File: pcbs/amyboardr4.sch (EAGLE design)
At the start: 126 parts, among them J1 52601-G10-8LF, Q2 S8050, Q5 S8050, U1 PCM9211PT, U13 HX3608, U15 H11L1SR2M, U16 SPX3819, U2 ESP32­S2­SOLO, Y1 22.5792MHZ

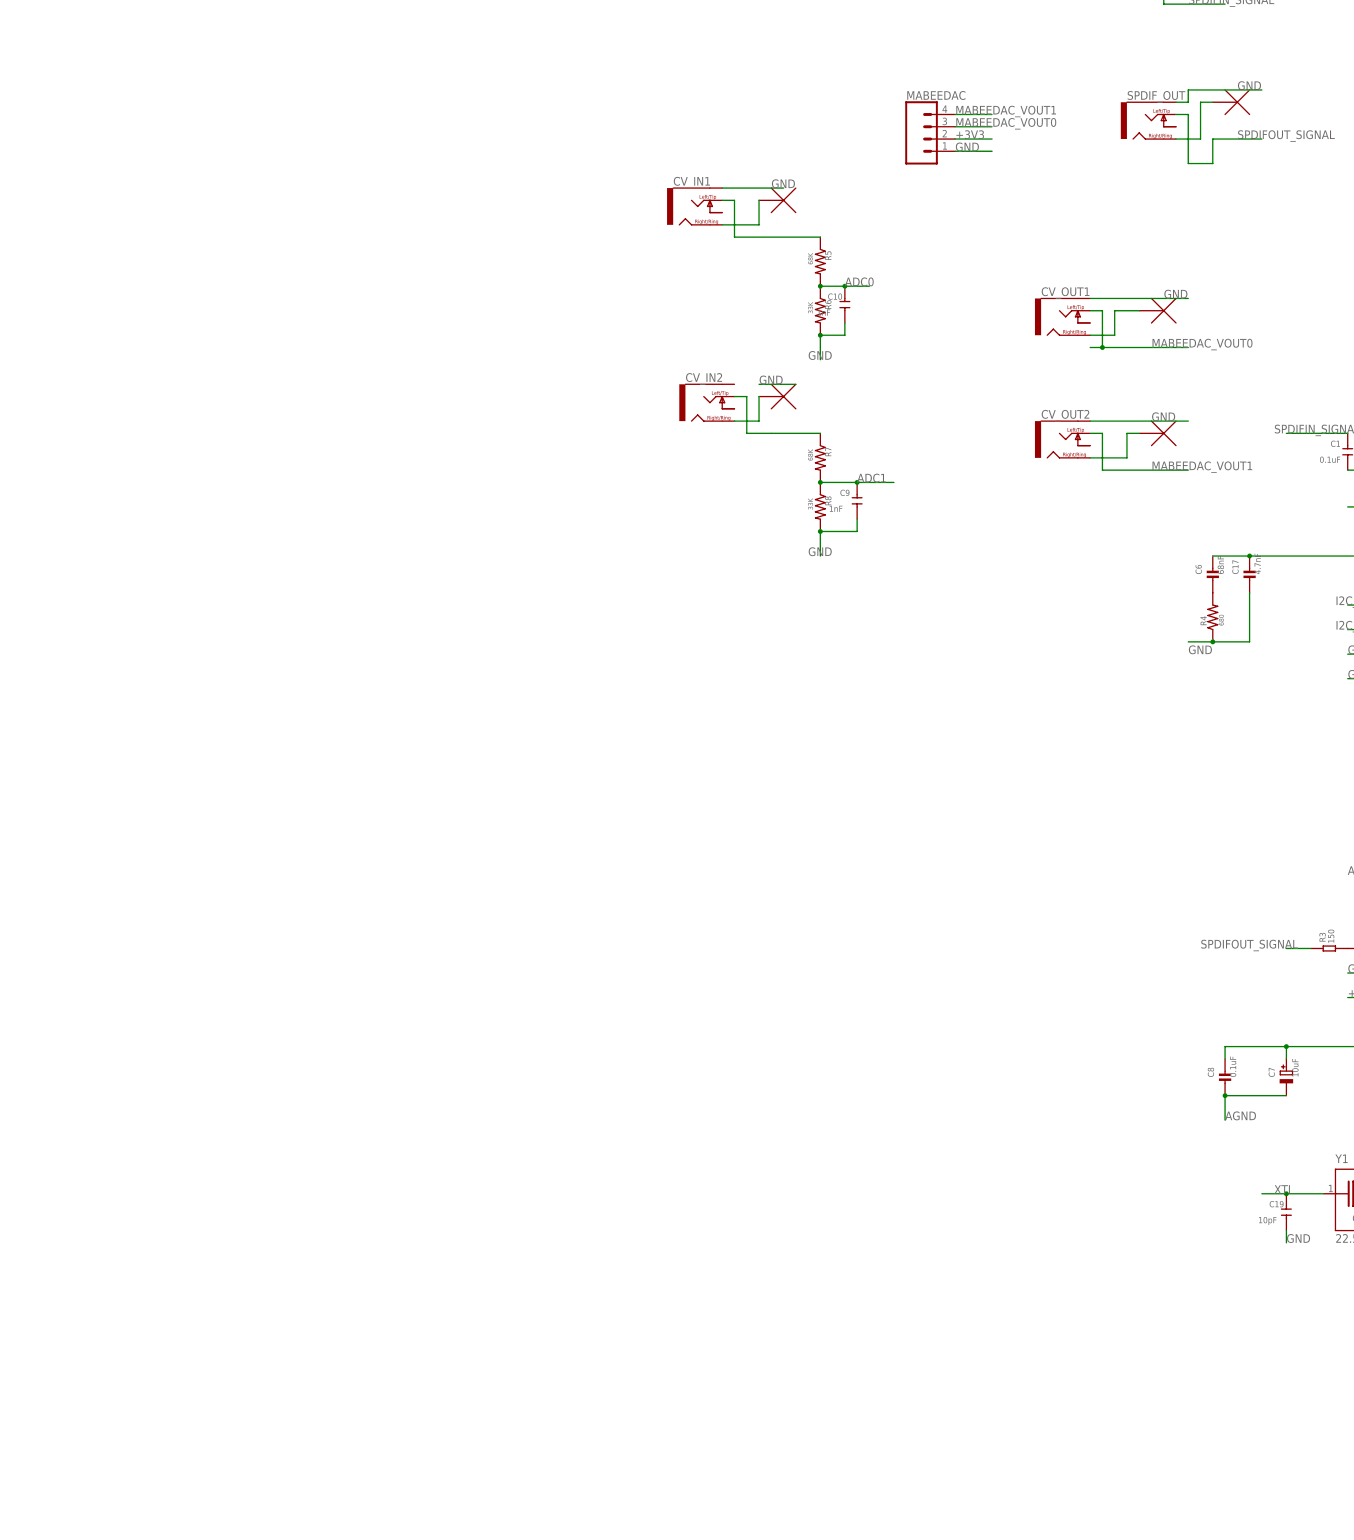
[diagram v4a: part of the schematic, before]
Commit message: adding parts for amyboard
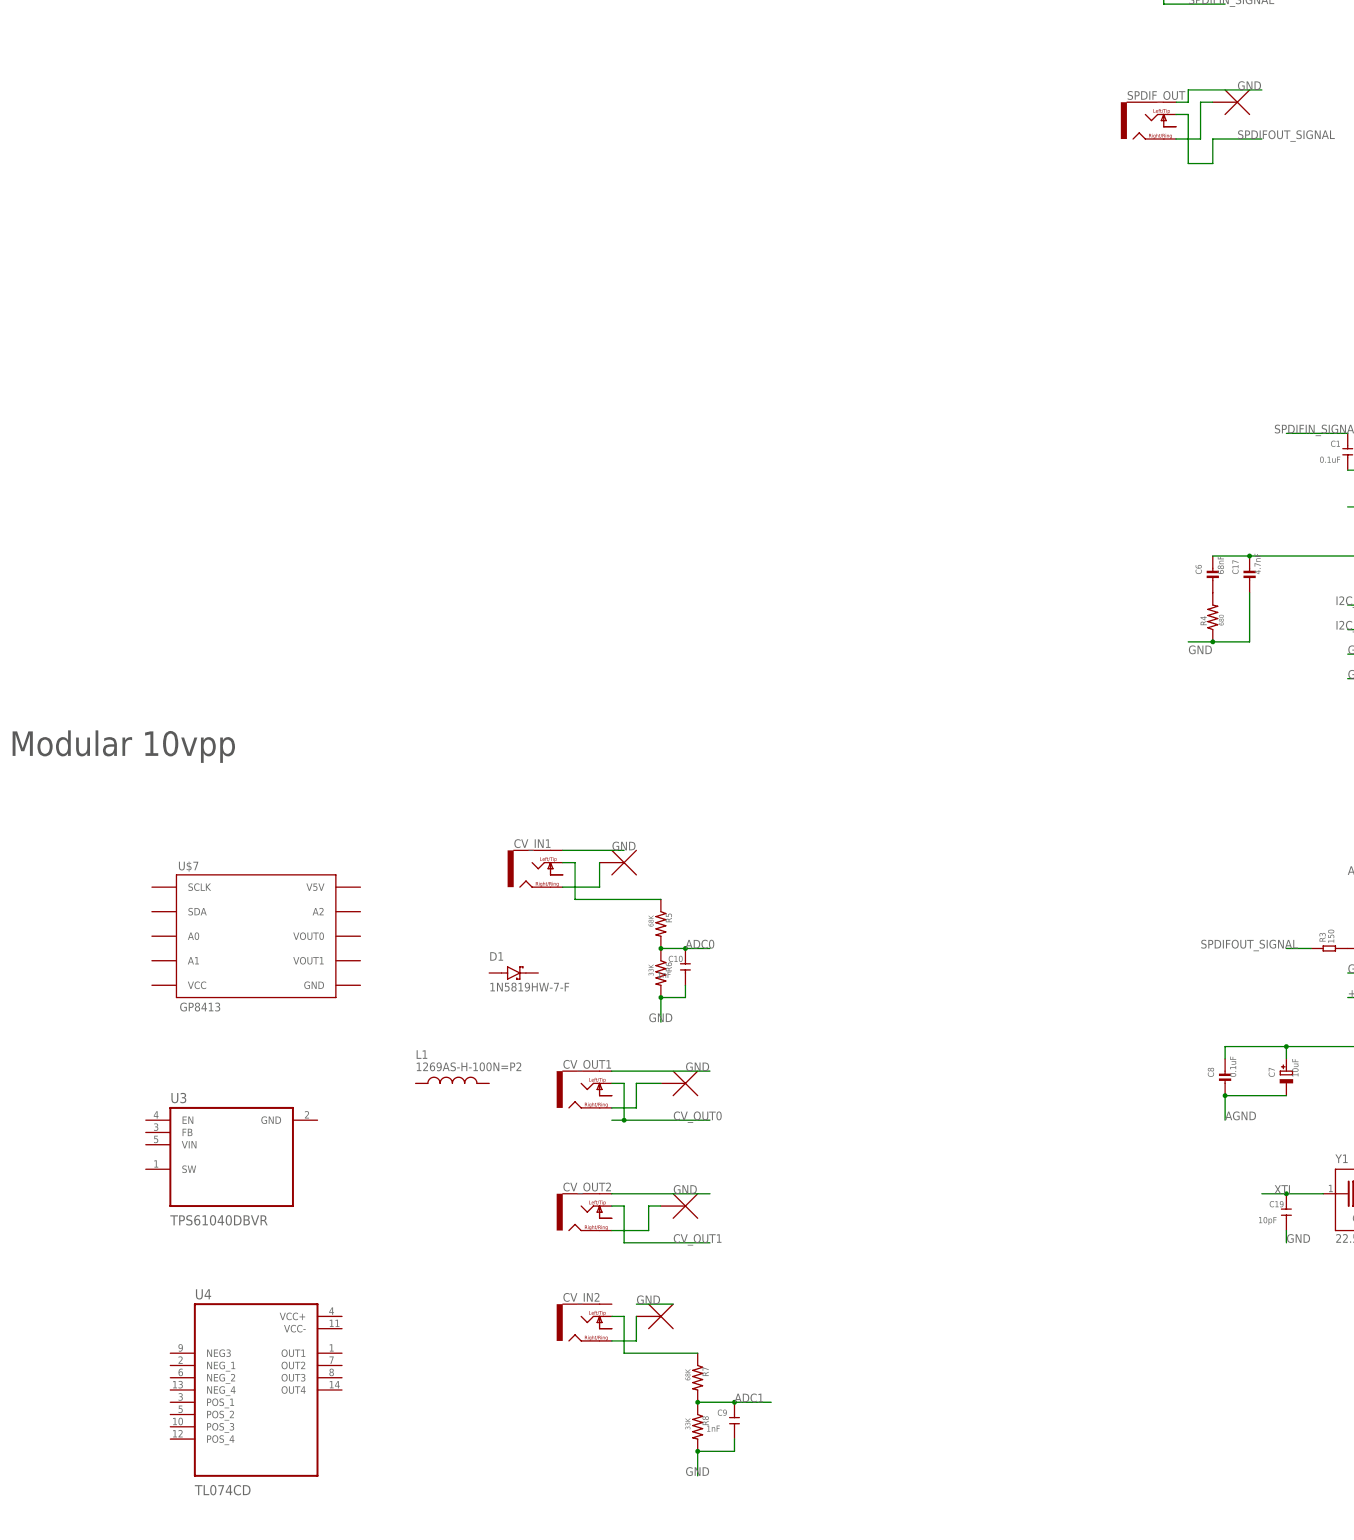
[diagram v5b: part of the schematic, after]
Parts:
- removed MABEEDAC: (no value), SparkFun-Connectors:CONN_04
- added D1: 1N5819HW-7-F, 1N5819HW-7-F:1N5819HW-7-F
- added L1: 1269AS-H-100N=P2, 1269AS-H-100N_P2:1269AS-H-100N=P2
- added U$7: GP8413, FL5160MX:GP8413
- added U3: TPS61040DBVR, TPS61040DBVR:TPS61040DBVR
- added U4: TL074CD, TL074CD:TL074CD
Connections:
- removed net MABEEDAC_VOUT0: CV_OUT1.TIP, MABEEDAC.3
- removed net MABEEDAC_VOUT1: CV_OUT2.TIP, MABEEDAC.4
- new net CV_OUT0: CV_OUT1.TIP
- new net CV_OUT1: CV_OUT2.TIP
- net +3V3: no longer MABEEDAC.2
- net GND: no longer MABEEDAC.1
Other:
- note added: "Modular 10vpp"
- moved on the sheet: C10, C9, CV_IN1, CV_IN2, CV_OUT1, CV_OUT2, R5, R6, R7, R8

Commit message: Added 8413, TL074, DIP switch, +/-12V rails to schematic.
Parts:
- removed D1: 1N5819HW-7-F, 1N5819HW-7-F:1N5819HW-7-F
- removed L1: 1269AS-H-100N=P2, 1269AS-H-100N_P2:1269AS-H-100N=P2
- removed U3: TPS61040DBVR, TPS61040DBVR:TPS61040DBVR
- added C20, C28: 100nF, Discrete-new:CAP-0603
- added C21: 20pF, Discrete-new:CAP-0603
- added C22: 1uF, microbuilder:CAP_ELECTROLYTICPANASONIC_C
- added C23, C24, C26, C33: 0.1uF, microbuilder:CAP_CERAMIC0805-NOOUTLINE
- added C25, C29: 22pF, Discrete-new:CAP-0603
- added C27, C30, C31: 22uF, Discrete-new:CAP-0603
- added C32: 10uF, microbuilder:CAP_ELECTROLYTICPANASONIC_C
- added D10, D8, D9: SS54, diode:DIODE-DO-214AC
- added D4, D5, D6: 1N5819HW-7-F, 1N5819HW-7-F:1N5819HW-7-F
- added L2: 1269AS-H-100N=P2, 1269AS-H-100N_P2:1269AS-H-100N=P2
- added L3: 3.3µH/±30%/3.4A, SparkFun-Coils:INDUCTOR-CR54-3.3UH
- added R10, R11, R22: 30K, adafruit:R-US_R0805
- added R12: 1M, A9G:DISCRETE_R-0603
- added R13: 115K, A9G:DISCRETE_R-0603
- added R14: 100K, A9G:DISCRETE_R-0603
- added R15, R16: NC, A9G:DISCRETE_R-0603
- added R17: 0R, A9G:DISCRETE_R-0603
- added R18: 228K, A9G:DISCRETE_R-0603
- added R19: 12K, A9G:DISCRETE_R-0603
- added R20, R23, R24: 10K, adafruit:R-US_R0805
- added R21: 15K, adafruit:R-US_R0805
- added R25, R26, R29, R30: 22K, adafruit:R-US_R0805
- added R27, R28: 51K, adafruit:R-US_R0805
- added S1: SWS008, smd-special:SWS008
- added U5: TPS61040DBVR, TPS61040DBVR:TPS61040DBVR
- added U6: HX3608, self:HX3608
- R1, R2: value 10K -> 51K
- R5: value 68K -> 10K
- R6: value 33K -> 15K
- R7: value 68K -> 30K
- R8: value 33K -> 30K
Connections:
- removed net CV_OUT0: CV_OUT1.TIP
- new net 12V: C27.1, C28.1, C29.1, D8.C, R17.2, R18.2
- new net ADC2: C9.1, R7.2, S1.10
- new net CV_OUT2: CV_OUT2.TIP, R10.2, R11.2, U4.OUT2
- new net LOUT_2V: C97.1, R79.1, U4.POS_3
- new net N$15: R20.2, R21.1, S1.7
- new net N$16: R5.2, R6.1, S1.8
- new net N$18: C24.1, U$7.VOUT0, U4.POS_1
- new net N$20: C23.1, U$7.VOUT1, U4.POS_2
- new net N$21: C30.1, D8.A, L3.2, U6.SW
- new net N$22: C22.+, U$7.V5V
- new net N$23: D4.A, L2.1, U5.SW
- new net N$24: C25.1, D4.K, R12.2
- new net N$25: C25.2, R12.1, R13.2, U5.FB
- new net N$26: C29.2, R18.1, R19.2, U6.FB
- new net N$27: R15.2, U6.NC
- new net N$28: R16.1, R17.1, U6.VIN
- new net N$29: C30.2, D10.C, D9.A
- new net N$30: R23.1, S1.6
- new net N$31: R10.1, R11.1, S1.12, U4.NEG_2
- new net N$32: R24.1, S1.5
- new net N$33: R22.1, S1.11, U4.NEG_1
- new net N$35: R26.1, S1.1
- new net N$36: R25.1, S1.2
- new net N$40: R29.1, S1.4
- new net N$41: R30.1, S1.3
- new net N$44: R27.1, S1.15, U4.NEG3
- new net N$45: R28.1, S1.16, U4.NEG_4
- new net ROUT_2V: C96.1, R78.1, U4.POS_4
- net +12V: now also C21.1, C26.1, U$7.VCC, U4.VCC+
- net +3V3: now also C32.+, C33.1, L2.2, R20.1, R23.2, R24.2, R5.1, U5.EN, U5.VIN
- net -12V: now also C20.2, C21.2, C31.2, D10.A, U4.VCC-
- net ADC0: no longer C10.1, R5.2, R6.1
- net ADC1: now also C10.1, R8.2, S1.9; no longer C9.1, R7.2, R8.1
- net AGND: now also C32.-, C33.2, R25.2, R26.2, R29.2, R30.2
- net CV_OUT1: now also CV_OUT1.TIP, R22.2, U4.OUT1; no longer CV_OUT2.TIP
- net ENABLE: now also R14.1, U6.EN
- net GND: now also C20.1, C22.-, C23.2, C24.2, C26.2, C27.2, C28.2, C31.1, D9.C, R13.1, R15.1, R19.1, R21.2, U$7.A0, U$7.A1, U$7.A2, U$7.GND, U5.GND, U6.GND; no longer R8.2
- net I2C_SCL: now also U$7.SCLK
- net I2C_SDA: now also U$7.SDA
- net LIN: now also R2.2; no longer C2.-
- net LINX: now also C2.+; no longer R2.2
- net LOUT: now also R27.2, U4.OUT3; no longer C97.1, R79.1
- net N$17: now also R8.1; no longer R5.1
- net N$4: now also C2.-, S1.13; no longer C2.+
- net N$5: now also C3.-, R1.1, S1.14; no longer C3.+, R1.2
- net RIN: now also R1.2; no longer C3.-
- net RINX: now also C3.+; no longer R1.1
- net ROUT: now also R28.2, U4.OUT4; no longer C96.1, R78.1
- net VPWR: now also L3.1, R14.2, R16.2
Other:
- moved on the sheet: C10, C2, C3, C9, CV_IN1, CV_IN2, CV_OUT1, CV_OUT2, R1, R2, R5, R6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

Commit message: removing other boost
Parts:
- removed C25: 22pF, Discrete-new:CAP-0603
- removed D4, D5, D6: 1N5819HW-7-F, 1N5819HW-7-F:1N5819HW-7-F
- removed L2: 1269AS-H-100N=P2, 1269AS-H-100N_P2:1269AS-H-100N=P2
- removed R12: 1M, A9G:DISCRETE_R-0603
- removed R13: 115K, A9G:DISCRETE_R-0603
- removed U5: TPS61040DBVR, TPS61040DBVR:TPS61040DBVR
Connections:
- removed net N$23: D4.A, L2.1, U5.SW
- removed net N$24: C25.1, D4.K, R12.2
- removed net N$25: C25.2, R12.1, R13.2, U5.FB
- net +3V3: no longer L2.2, U5.EN, U5.VIN
- net GND: no longer R13.1, U5.GND
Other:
- note added: "NOTES/TODO: - NC/GND unused pins - 12V -> 5V regulator for modular port - Confirm VOUT / VPWR / 3v3 / 5v / 12V"
- note removed: "NOTES/TODO: - MabeeDAC to provide VOUT0 and VOUT1 - NC/GND unused pins - 12V -> 5V regulator for modular port - Confirm VOUT / VPWR / 3v3 / 5v / 12V"
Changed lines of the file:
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@@
 <part name="U$7" library="FL5160MX" deviceset="GP8413" device=""/>
 <part name="U4" library="TL074CD" deviceset="TL074CD" device=""/>
-<part name="U5" library="TPS61040DBVR" deviceset="TPS61040DBVR" device=""/>
-<part name="L2" library="1269AS-H-100N_P2" deviceset="1269AS-H-100N=P2" device=""/>
-<part name="D4" library="1N5819HW-7-F" deviceset="1N5819HW-7-F" device=""/>
-<part name="R12" library="A9G" deviceset="DISCRETE_R*" device="-0603" value="1M"/>
-<part name="R13" library="A9G" deviceset="DISCRETE_R*" device="-0603" value="115K"/>
-<part name="C25" library="Discrete-new" deviceset="CAP" device="-0603" value="22pF"/>
-<part name="D5" library="1N5819HW-7-F" deviceset="1N5819HW-7-F" device=""/>
-<part name="D6" library="1N5819HW-7-F" deviceset="1N5819HW-7-F" device=""/>
 <part name="U6" library="self" deviceset="HX3608" device=""/>
 <part name="D8" library="diode" deviceset="DIODE-" device="DO-214AC" value="SS54"/>
@@
 <text x="192.786" y="113.538" size="5.08" layer="97">HEADERS</text>
 <text x="294.64" y="190.5" size="3.81" layer="97">NOTES/TODO:
-- MabeeDAC to provide VOUT0 and VOUT1
 - NC/GND unused pins
 - 12V -&gt; 5V regulator for modular port
@@
 <attribute name="VALUE" x="-223.52" y="-52.26" size="2.0828" layer="96" ratio="10" rot="SR0"/>
 </instance>
-<instance part="U5" gate="A" x="7.62" y="-172.72" smashed="yes" rot="R90">
-<attribute name="NAME" x="-3.54" y="-185.42" size="2.0828" layer="95" ratio="10" rot="SR90"/>
-<attribute name="VALUE" x="21.78" y="-185.42" size="2.0828" layer="96" ratio="10" rot="SR90"/>
-</instance>
-<instance part="L2" gate="G$1" x="5.08" y="-205.74" smashed="yes" rot="R90">
-<attribute name="NAME" x="0" y="-213.36" size="1.778" layer="95" rot="R90"/>
-<attribute name="VALUE" x="2.54" y="-213.36" size="1.778" layer="96" rot="R90"/>
-</instance>
-<instance part="D4" gate="G$1" x="5.08" y="-218.44" smashed="yes" rot="R270">
-<attribute name="NAME" x="7.62" y="-213.36" size="1.778" layer="95" rot="R270"/>
-<attribute name="VALUE" x="1.27" y="-213.36" size="1.778" layer="96" rot="R270"/>
-</instance>
-<instance part="R12" gate="R" x="10.16" y="-232.41" smashed="yes" rot="R180">
-<attribute name="NAME" x="10.16" y="-233.68" size="1.27" layer="95" ratio="10" rot="R270"/>
-<attribute name="VALUE" x="9.144" y="-233.426" size="1.27" layer="96" ratio="10" rot="R270"/>
-</instance>
-<instance part="R13" gate="R" x="17.78" y="-232.41" smashed="yes" rot="R180">
-<attribute name="NAME" x="17.78" y="-233.68" size="1.27" layer="95" ratio="10" rot="R270"/>
-<attribute name="VALUE" x="16.764" y="-233.426" size="1.27" layer="96" ratio="10" rot="R270"/>
-</instance>
-<instance part="C25" gate="C" x="11.43" y="-223.52" smashed="yes">
-<attribute name="NAME" x="10.414" y="-227.076" size="1.27" layer="95" ratio="10" rot="R90"/>
-<attribute name="VALUE" x="13.716" y="-229.362" size="1.27" layer="96" ratio="10" rot="R90"/>
-</instance>
-<instance part="D5" gate="G$1" x="35.56" y="-254" smashed="yes" rot="R270">
-<attribute name="NAME" x="38.1" y="-254" size="1.778" layer="95" rot="R270"/>
-<attribute name="VALUE" x="31.75" y="-248.92" size="1.778" layer="96" rot="R270"/>
-</instance>
-<instance part="D6" gate="G$1" x="45.72" y="-259.08" smashed="yes">
-<attribute name="NAME" x="40.64" y="-256.54" size="1.778" layer="95"/>
-<attribute name="VALUE" x="40.64" y="-262.89" size="1.778" layer="96"/>
-</instance>
 <instance part="U6" gate="G$1" x="261.62" y="-91.44" smashed="yes">
 <attribute name="NAME" x="259.08" y="-104.14" size="1.778" layer="95"/>
@@
 </segment>
 <segment>
-<pinref part="U5" gate="A" pin="GND"/>
-<wire x1="10.16" y1="-154.94" x2="0" y2="-154.94" width="0.1524" layer="91"/>
-<label x="12.7" y="-154.94" size="1.778" layer="95" rot="R90"/>
-</segment>
-<segment>
-<pinref part="R13" gate="R" pin="1"/>
-<wire x1="21.59" y1="-232.41" x2="27.94" y2="-232.41" width="0.1524" layer="91"/>
-<wire x1="27.94" y1="-232.41" x2="27.94" y2="-231.14" width="0.1524" layer="91"/>
-<label x="27.94" y="-231.14" size="1.778" layer="95" rot="R90"/>
-<wire x1="27.94" y1="-231.14" x2="27.94" y2="-223.52" width="0.1524" layer="91"/>
-</segment>
-<segment>
 <wire x1="247.65" y1="-97.79" x2="247.65" y2="-93.98" width="0.1524" layer="91"/>
 <pinref part="U6" gate="G$1" pin="GND"/>
@@
 </segment>
 <segment>
-<pinref part="U5" gate="A" pin="VIN"/>
-<wire x1="5.08" y1="-190.5" x2="5.08" y2="-198.12" width="0.1524" layer="91"/>
-<wire x1="5.08" y1="-198.12" x2="0" y2="-198.12" width="0.1524" layer="91"/>
-<pinref part="U5" gate="A" pin="EN"/>
-<wire x1="0" y1="-190.5" x2="0" y2="-198.12" width="0.1524" layer="91"/>
-<wire x1="0" y1="-198.12" x2="-5.08" y2="-198.12" width="0.1524" layer="91"/>
-<junction x="0" y="-198.12"/>
-<label x="-5.08" y="-198.12" size="1.778" layer="95" rot="R90"/>
-<pinref part="L2" gate="G$1" pin="2"/>
-<junction x="5.08" y="-198.12"/>
-</segment>
-<segment>
 <pinref part="R5" gate="G$1" pin="1"/>
 <wire x1="-88.9" y1="27.94" x2="-88.9" y2="30.48" width="0.1524" layer="91"/>
@@
 </segment>
 </net>
-<net name="N$23" class="0">
-<segment>
-<pinref part="L2" gate="G$1" pin="1"/>
-<pinref part="D4" gate="G$1" pin="A"/>
-<pinref part="U5" gate="A" pin="SW"/>
-<wire x1="10.16" y1="-190.5" x2="10.16" y2="-213.36" width="0.1524" layer="91"/>
-<wire x1="10.16" y1="-213.36" x2="5.08" y2="-213.36" width="0.1524" layer="91"/>
-<junction x="5.08" y="-213.36"/>
-</segment>
-</net>
-<net name="N$24" class="0">
-<segment>
-<pinref part="R12" gate="R" pin="2"/>
-<pinref part="D4" gate="G$1" pin="K"/>
-<wire x1="6.35" y1="-232.41" x2="3.81" y2="-231.14" width="0.1524" layer="91"/>
-<wire x1="3.81" y1="-231.14" x2="5.08" y2="-223.52" width="0.1524" layer="91"/>
-<pinref part="C25" gate="C" pin="1"/>
-<wire x1="7.62" y1="-223.52" x2="5.08" y2="-231.14" width="0.1524" layer="91"/>
-<wire x1="5.08" y1="-231.14" x2="6.35" y2="-231.14" width="0.1524" layer="91"/>
-<wire x1="6.35" y1="-231.14" x2="6.35" y2="-232.41" width="0.1524" layer="91"/>
-<junction x="6.35" y="-232.41"/>
-</segment>
-</net>
-<net name="N$25" class="0">
-<segment>
-<pinref part="R12" gate="R" pin="1"/>
-<pinref part="R13" gate="R" pin="2"/>
-<wire x1="13.97" y1="-232.41" x2="13.97" y2="-190.5" width="0.1524" layer="91"/>
-<junction x="13.97" y="-232.41"/>
-<pinref part="U5" gate="A" pin="FB"/>
-<wire x1="13.97" y1="-190.5" x2="2.54" y2="-190.5" width="0.1524" layer="91"/>
-<pinref part="C25" gate="C" pin="2"/>
-<wire x1="15.24" y1="-223.52" x2="13.97" y2="-226.06" width="0.1524" layer="91"/>
-<wire x1="15.24" y1="-226.06" x2="13.97" y2="-226.06" width="0.1524" layer="91"/>
-<wire x1="13.97" y1="-226.06" x2="13.97" y2="-232.41" width="0.1524" layer="91"/>
-</segment>
-</net>
